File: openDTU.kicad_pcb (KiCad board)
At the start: 2 copper layers, 50 x 50 mm, 12 parts, among them U1 ESP32NodeMCU, U2 NRF24L01+PA+LNA_Breakout

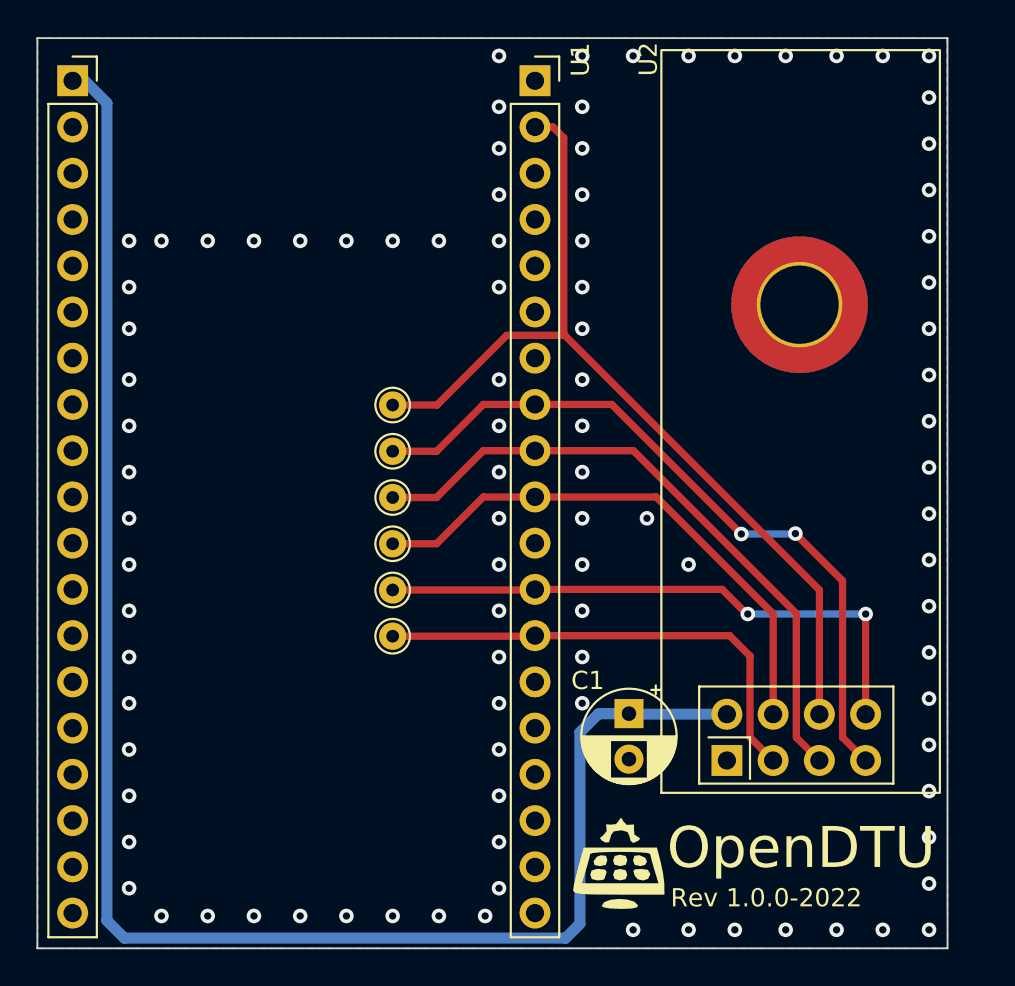
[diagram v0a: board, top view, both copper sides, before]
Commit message: adding first SMT parts to schematic and PCB, like MCU and nRF24L01+
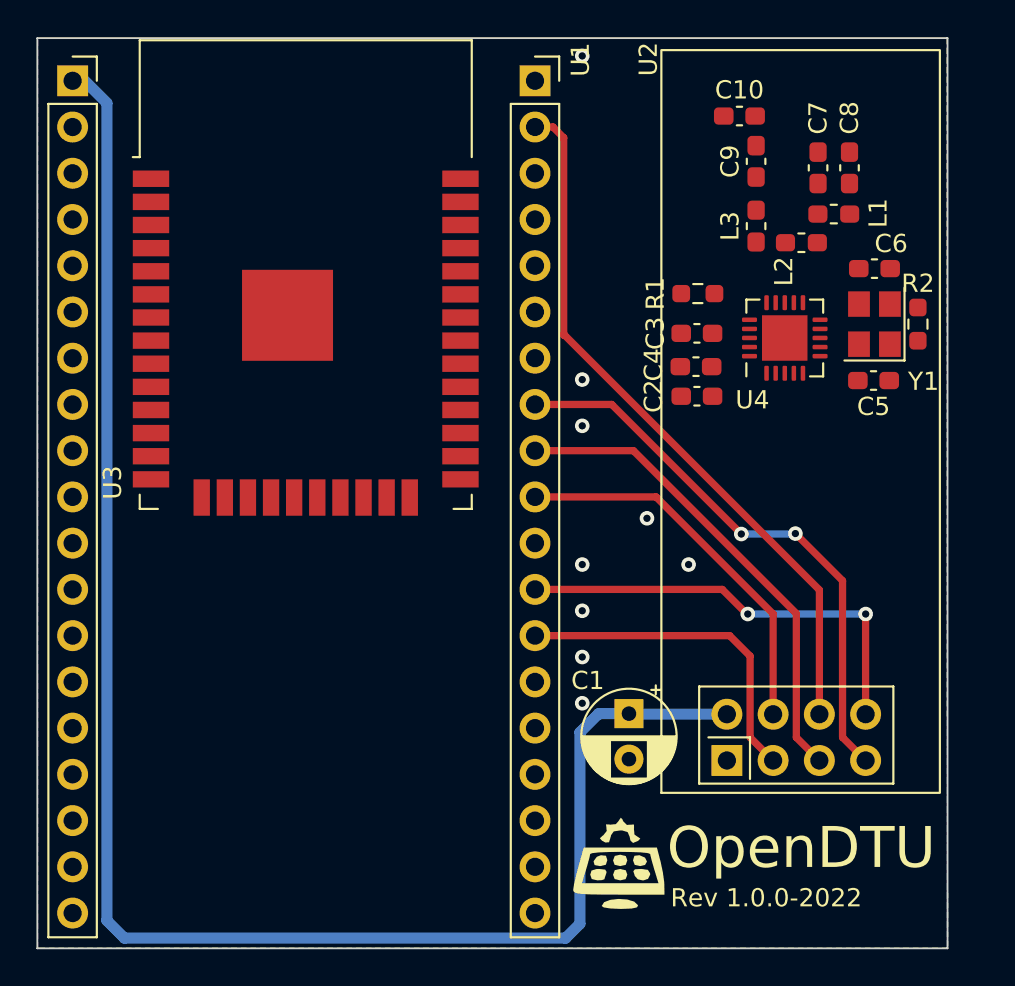
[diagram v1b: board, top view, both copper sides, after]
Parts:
- removed REF**: MountingHole_4.3mm_M4_DIN965_Pad_TopBottom, MountingHole:MountingHole_4.3mm_M4_DIN965_Pad_TopBottom
- removed REF**: KiCad-Logo2_5mm_SilkScreen, Symbol:KiCad-Logo2_5mm_SilkScreen
- removed TP1, TP2, TP3, TP4, TP5, TP6: TestPoint, TestPoint:TestPoint_THTPad_D1.5mm_Drill0.7mm
- added C10: 1pF, Capacitor_SMD:C_0603_1608Metric_Pad1.08x0.95mm_HandSolder, F.Cu at (158.8, 74.7)
- added C2: 10nF, Capacitor_SMD:C_0603_1608Metric_Pad1.08x0.95mm_HandSolder, F.Cu at (156.4, 90.1)
- added C3: 10nF, Capacitor_SMD:C_0603_1608Metric_Pad1.08x0.95mm_HandSolder, F.Cu at (156.4, 86.6)
- added C4: 33nF, Capacitor_SMD:C_0603_1608Metric_Pad1.08x0.95mm_HandSolder, F.Cu at (156.4, 88.4)
- added C5: 22pF, Capacitor_SMD:C_0603_1608Metric_Pad1.08x0.95mm_HandSolder, F.Cu at (166.1, 89.2)
- added C6: 22pF, Capacitor_SMD:C_0603_1608Metric_Pad1.08x0.95mm_HandSolder, F.Cu at (166.2, 83.1)
- added C7: 4.7pF, Capacitor_SMD:C_0603_1608Metric_Pad1.08x0.95mm_HandSolder, F.Cu at (163.1, 77.5)
- added C8: 2.2nF, Capacitor_SMD:C_0603_1608Metric_Pad1.08x0.95mm_HandSolder, F.Cu at (164.8, 77.5)
- added C9: 1.5pF, Capacitor_SMD:C_0603_1608Metric_Pad1.08x0.95mm_HandSolder, F.Cu at (159.7, 77.2)
- added L1: 2.7nH, Inductor_SMD:L_0603_1608Metric_Pad1.05x0.95mm_HandSolder, F.Cu at (163.9, 80.1)
- added L2: 8.2nH, Inductor_SMD:L_0603_1608Metric_Pad1.05x0.95mm_HandSolder, F.Cu at (162.2, 81.6)
- added L3: 3.9nH, Inductor_SMD:L_0603_1608Metric_Pad1.05x0.95mm_HandSolder, F.Cu at (159.7, 80.7)
- added R1: 22K, Resistor_SMD:R_0603_1608Metric_Pad0.98x0.95mm_HandSolder, F.Cu at (156.5, 84.4)
- added R2: 1M, Resistor_SMD:R_0603_1608Metric_Pad0.98x0.95mm_HandSolder, F.Cu at (168.6, 86.1)
- added U3: ESP32-WROOM-32, RF_Module:ESP32-WROOM-32, F.Cu at (134.9, 86.4)
- added U4: nRF24L01P, Package_DFN_QFN:QFN-20-1EP_4x4mm_P0.5mm_EP2.5x2.5mm, F.Cu at (161.2, 86.9)
- added Y1: Crystal, Crystal:Crystal_SMD_3225-4Pin_3.2x2.5mm, F.Cu at (166.2, 86.1)
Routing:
- net /MOSI: track 50.4 -> 39.3 mm
- net /SCK: track 35.5 -> 26.6 mm
- net /~{CSN}: track 30.1 -> 21.3 mm
- net /MISO: track 40.2 -> 31.3 mm
- net /CE: track 26.4 -> 18.6 mm
- net /IRQ: track 32.1 -> 24.3 mm
- net GND: vias 97 -> 9

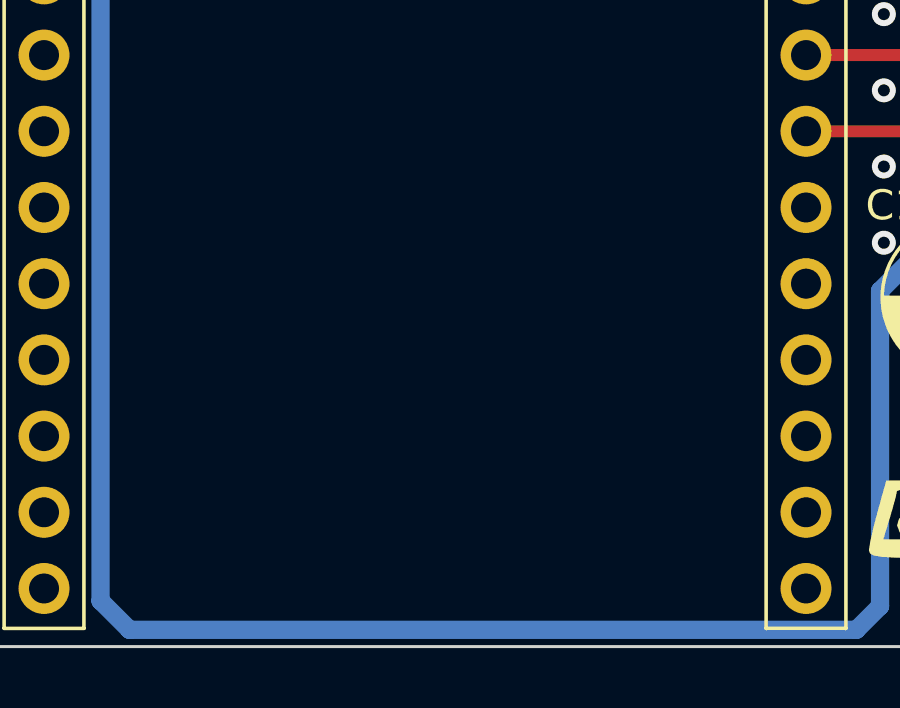
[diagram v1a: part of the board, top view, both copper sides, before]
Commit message: adding USB-C connector for power supply
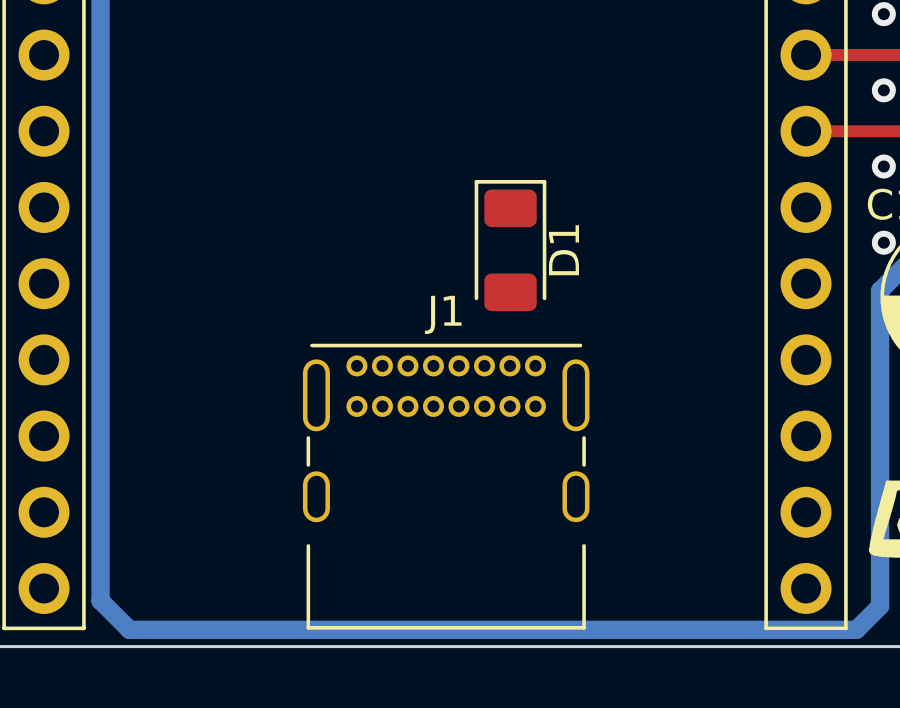
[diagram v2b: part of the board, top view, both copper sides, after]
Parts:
- added D1: D_Schottky, Diode_SMD:D_1206_3216Metric, F.Cu at (137.7, 107.2)
- added J1: USB_C_Receptacle_USB2.0, Connector_USB:USB_C_Receptacle_GCT_USB4085, F.Cu at (132.6, 111.0)
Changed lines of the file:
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@@
   (net 73 "Net-(C9-Pad1)")
   (net 74 "Net-(C10-Pad2)")
+  (net 75 "+5V")
+  (net 76 "VBUS")
+  (net 77 "unconnected-(J1-PadA5)")
+  (net 78 "unconnected-(J1-PadA6)")
+  (net 79 "unconnected-(J1-PadA7)")
+  (net 80 "unconnected-(J1-PadA8)")
+  (net 81 "unconnected-(J1-PadB5)")
+  (net 82 "unconnected-(J1-PadB6)")
+  (net 83 "unconnected-(J1-PadB7)")
+  (net 84 "unconnected-(J1-PadB8)")
   (footprint "Package_DFN_QFN:QFN-20-1EP_4x4mm_P0.5mm_EP2.5x2.5mm" (layer "F.Cu")
     (at 161.2392 86.868 90)
@@
       (scale (xyz 1 1 1))
       (rotate (xyz -90 0 0))
+    )
+  )
+  (footprint "Diode_SMD:D_1206_3216Metric" (layer "F.Cu")
+    (at 137.668 107.188 -90)
+    (descr "Diode SMD 1206 (3216 Metric), square (rectangular) end terminal, IPC_7351 nominal, (Body size source: http://www.tortai-tech.com/upload/download/2011102023233369053.pdf), generated with kicad-footprint-generator")
+    (tags "diode")
+    (property "Sheetfile" "File: openDTU.kicad_sch")
+    (property "Sheetname" "")
+    (attr smd)
+    (fp_text reference "D1" (at 0 -1.82 90) (layer "F.SilkS")
+      (effects (font (size 1 1) (thickness 0.15)))
+    )
+    (fp_text value "D_Schottky" (at 0 1.82 90) (layer "F.Fab")
+      (effects (font (size 1 1) (thickness 0.15)))
+    )
+    (fp_text user "${REFERENCE}" (at 0 0 90) (layer "F.Fab")
+      (effects (font (size 0.8 0.8) (thickness 0.12)))
+    )
+    (fp_line (start -2.285 -1.135) (end -2.285 1.135) (layer "F.SilkS") (width 0.12))
+    (fp_line (start -2.285 1.135) (end 1.6 1.135) (layer "F.SilkS") (width 0.12))
+    (fp_line (start 1.6 -1.135) (end -2.285 -1.135) (layer "F.SilkS") (width 0.12))
+    (fp_line (start 2.28 1.12) (end -2.28 1.12) (layer "F.CrtYd") (width 0.05))
+    (fp_line (start -2.28 1.12) (end -2.28 -1.12) (layer "F.CrtYd") (width 0.05))
+    (fp_line (start -2.28 -1.12) (end 2.28 -1.12) (layer "F.CrtYd") (width 0.05))
+    (fp_line (start 2.28 -1.12) (end 2.28 1.12) (layer "F.CrtYd") (width 0.05))
+    (fp_line (start -1.6 -0.4) (end -1.6 0.8) (layer "F.Fab") (width 0.1))
+    (fp_line (start 1.6 0.8) (end 1.6 -0.8) (layer "F.Fab") (width 0.1))
+    (fp_line (start -1.6 0.8) (end 1.6 0.8) (layer "F.Fab") (width 0.1))
+    (fp_line (start -1.2 -0.8) (end -1.6 -0.4) (layer "F.Fab") (width 0.1))
+    (fp_line (start 1.6 -0.8) (end -1.2 -0.8) (layer "F.Fab") (width 0.1))
+    (pad "1" smd roundrect (at -1.4 0 270) (size 1.25 1.75) (layers "F.Cu" "F.Paste" "F.Mask") (roundrect_rratio 0.2)
+      (net 75 "+5V") (pinfunction "K") (pintype "passive"))
+    (pad "2" smd roundrect (at 1.4 0 270) (size 1.25 1.75) (layers "F.Cu" "F.Paste" "F.Mask") (roundrect_rratio 0.2)
+      (net 76 "VBUS") (pinfunction "A") (pintype "passive"))
+    (model "${KICAD6_3DMODEL_DIR}/Diode_SMD.3dshapes/D_1206_3216Metric.wrl"
+      (offset (xyz 0 0 0))
+      (scale (xyz 1 1 1))
+      (rotate (xyz 0 0 0))
     )
   )
@@
       (offset (xyz 0 0 0))
       (scale (xyz 1 1 1))
+      (rotate (xyz 0 0 0))
+    )
+  )
+  (footprint "Connector_USB:USB_C_Receptacle_GCT_USB4085" (layer "F.Cu")
+    (at 132.5504 111.0404)
+    (descr "USB 2.0 Type C Receptacle, https://gct.co/Files/Drawings/USB4085.pdf")
+    (tags "USB Type-C Receptacle Through-hole Right angle")
+    (property "Sheetfile" "File: openDTU.kicad_sch")
+    (property "Sheetname" "")
+    (attr through_hole)
+    (fp_text reference "J1" (at 2.975 -1.8) (layer "F.SilkS")
+      (effects (font (size 1 1) (thickness 0.15)))
+    )
+    (fp_text value "USB_C_Receptacle_USB2.0" (at 2.975 9.925) (layer "F.Fab")
+      (effects (font (size 1 1) (thickness 0.15)))
+    )
+    (fp_text user "PCB Edge" (at 2.975 6.1) (layer "Dwgs.User")
+      (effects (font (size 0.5 0.5) (thickness 0.1)))
+    )
+    (fp_text user "${REFERENCE}" (at 2.975 4.025) (layer "F.Fab")
+      (effects (font (size 1 1) (thickness 0.15)))
+    )
+    (fp_line (start -1.62 8.73) (end 7.57 8.73) (layer "F.SilkS") (width 0.12))
+    (fp_line (start 7.57 2.4) (end 7.57 3.3) (layer "F.SilkS") (width 0.12))
+    (fp_line (start 7.57 6) (end 7.57 8.73) (layer "F.SilkS") (width 0.12))
+    (fp_line (start -1.62 2.4) (end -1.62 3.3) (layer "F.SilkS") (width 0.12))
+    (fp_line (start -1.62 6) (end -1.62 8.73) (layer "F.SilkS") (width 0.12))
+    (fp_line (start -1.5 -0.68) (end 7.45 -0.68) (layer "F.SilkS") (width 0.12))
+    (fp_line (start -2.3 -1.06) (end -2.3 9.11) (layer "F.CrtYd") (width 0.05))
+    (fp_line (start 8.25 -1.06) (end 8.25 9.11) (layer "F.CrtYd") (width 0.05))
+    (fp_line (start -2.3 9.11) (end 8.25 9.11) (layer "F.CrtYd") (width 0.05))
+    (fp_line (start -2.3 -1.06) (end 8.25 -1.06) (layer "F.CrtYd") (width 0.05))
+    (fp_line (start -1.5 -0.56) (end 7.45 -0.56) (layer "F.Fab") (width 0.1))
+    (fp_line (start -0.025 6.1) (end 5.975 6.1) (layer "F.Fab") (width 0.1))
+    (fp_line (start -1.5 8.61) (end 7.45 8.61) (layer "F.Fab") (width 0.1))
+    (fp_line (start 7.45 -0.56) (end 7.45 8.61) (layer "F.Fab") (width 0.1))
+    (fp_line (start -1.5 -0.56) (end -1.5 8.61) (layer "F.Fab") (width 0.1))
+    (pad "A1" thru_hole circle (at 0 0) (size 0.7 0.7) (drill 0.4) (layers *.Cu *.Mask)
+      (net 14 "GND") (pinfunction "GND") (pintype "passive"))
+    (pad "A4" thru_hole circle (at 0.85 0) (size 0.7 0.7) (drill 0.4) (layers *.Cu *.Mask)
+      (net 76 "VBUS") (pinfunction "VBUS") (pintype "passive"))
+    (pad "A5" thru_hole circle (at 1.7 0) (size 0.7 0.7) (drill 0.4) (layers *.Cu *.Mask)
+      (net 77 "unconnected-(J1-PadA5)") (pinfunction "CC1") (pintype "bidirectional"))
+    (pad "A6" thru_hole circle (at 2.55 0) (size 0.7 0.7) (drill 0.4) (layers *.Cu *.Mask)
+      (net 78 "unconnected-(J1-PadA6)") (pinfunction "D+") (pintype "bidirectional"))
+    (pad "A7" thru_hole circle (at 3.4 0) (size 0.7 0.7) (drill 0.4) (layers *.Cu *.Mask)
+      (net 79 "unconnected-(J1-PadA7)") (pinfunction "D-") (pintype "bidirectional"))
+    (pad "A8" thru_hole circle (at 4.25 0) (size 0.7 0.7) (drill 0.4) (layers *.Cu *.Mask)
+      (net 80 "unconnected-(J1-PadA8)") (pinfunction "SBU1") (pintype "bidirectional"))
+    (pad "A9" thru_hole circle (at 5.1 0) (size 0.7 0.7) (drill 0.4) (layers *.Cu *.Mask)
+      (net 76 "VBUS") (pinfunction "VBUS") (pintype "passive"))
+    (pad "A12" thru_hole circle (at 5.95 0) (size 0.7 0.7) (drill 0.4) (layers *.Cu *.Mask)
+      (net 14 "GND") (pinfunction "GND") (pintype "passive"))
+    (pad "B1" thru_hole circle (at 5.95 1.35) (size 0.7 0.7) (drill 0.4) (layers *.Cu *.Mask)
+      (net 14 "GND") (pinfunction "GND") (pintype "passive"))
+    (pad "B4" thru_hole circle (at 5.1 1.35) (size 0.7 0.7) (drill 0.4) (layers *.Cu *.Mask)
+      (net 76 "VBUS") (pinfunction "VBUS") (pintype "passive"))
+    (pad "B5" thru_hole circle (at 4.25 1.35) (size 0.7 0.7) (drill 0.4) (layers *.Cu *.Mask)
+      (net 81 "unconnected-(J1-PadB5)") (pinfunction "CC2") (pintype "bidirectional"))
+    (pad "B6" thru_hole circle (at 3.4 1.35) (size 0.7 0.7) (drill 0.4) (layers *.Cu *.Mask)
+      (net 82 "unconnected-(J1-PadB6)") (pinfunction "D+") (pintype "bidirectional"))
+    (pad "B7" thru_hole circle (at 2.55 1.35) (size 0.7 0.7) (drill 0.4) (layers *.Cu *.Mask)
+      (net 83 "unconnected-(J1-PadB7)") (pinfunction "D-") (pintype "bidirectional"))
+    (pad "B8" thru_hole circle (at 1.7 1.35) (size 0.7 0.7) (drill 0.4) (layers *.Cu *.Mask)
+      (net 84 "unconnected-(J1-PadB8)") (pinfunction "SBU2") (pintype "bidirectional"))
+    (pad "B9" thru_hole circle (at 0.85 1.35) (size 0.7 0.7) (drill 0.4) (layers *.Cu *.Mask)
+      (net 76 "VBUS") (pinfunction "VBUS") (pintype "passive"))
+    (pad "B12" thru_hole circle (at 0 1.35) (size 0.7 0.7) (drill 0.4) (layers *.Cu *.Mask)
+      (net 14 "GND") (pinfunction "GND") (pintype "passive"))
+    (pad "S1" thru_hole oval (at -1.35 0.98) (size 0.9 2.4) (drill oval 0.6 2.1) (layers *.Cu *.Mask)
+      (net 14 "GND") (pinfunction "SHIELD") (pintype "passive"))
+    (pad "S1" thru_hole oval (at 7.3 4.36) (size 0.9 1.7) (drill oval 0.6 1.4) (layers *.Cu *.Mask)
+      (net 14 "GND") (pinfunction "SHIELD") (pintype "passive"))
+    (pad "S1" thru_hole oval (at -1.35 4.36) (size 0.9 1.7) (drill oval 0.6 1.4) (layers *.Cu *.Mask)
+      (net 14 "GND") (pinfunction "SHIELD") (pintype "passive"))
+    (pad "S1" thru_hole oval (at 7.3 0.98) (size 0.9 2.4) (drill oval 0.6 2.1) (layers *.Cu *.Mask)
+      (net 14 "GND") (pinfunction "SHIELD") (pintype "passive"))
+    (model "${KICAD6_3DMODEL_DIR}/Connector_USB.3dshapes/USB_C_Receptacle_GCT_USB4085.wrl"
+      (offset (xyz 0 0 0))
+      (scale (xyz 1 1 1))
